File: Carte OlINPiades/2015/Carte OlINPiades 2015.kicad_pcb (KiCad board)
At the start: 2 copper layers, 284 parts, among them U1 dsPIC33FJ128MC802, U2 LM7805, U3 LM2937-3.3

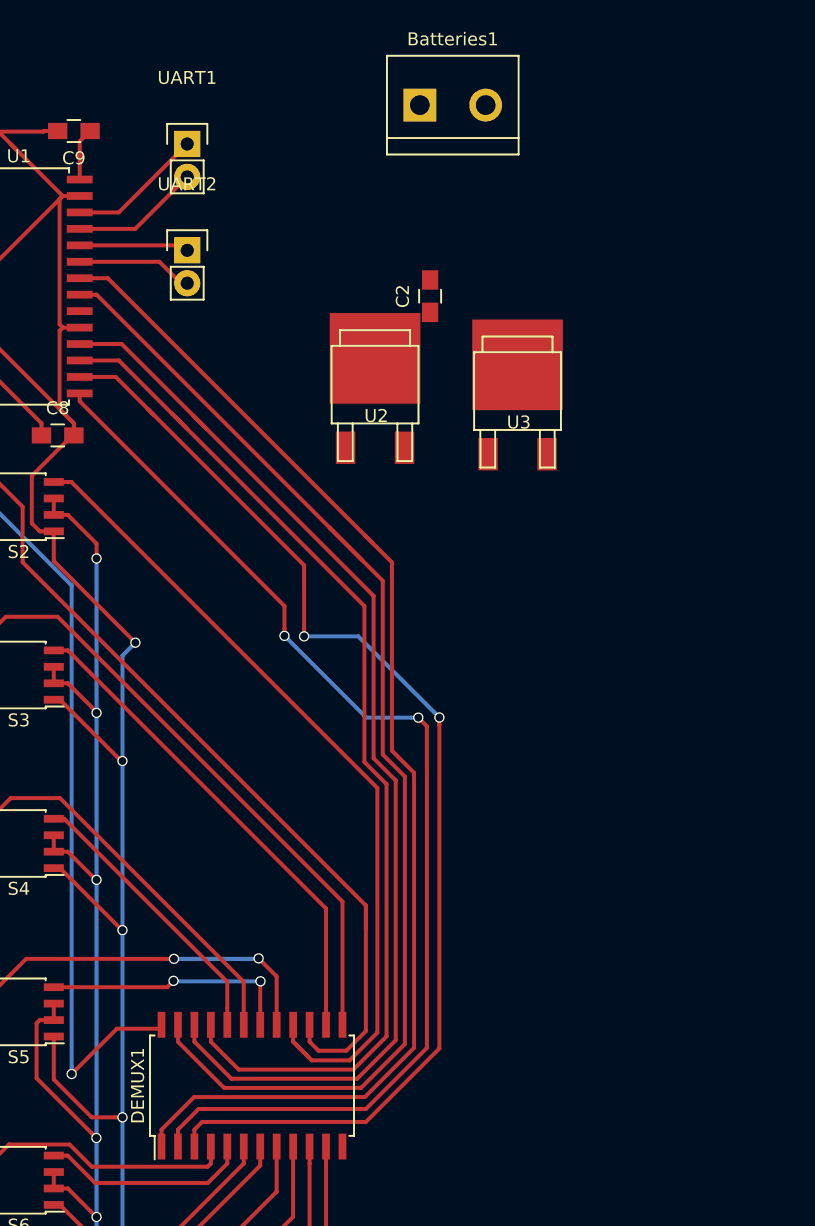
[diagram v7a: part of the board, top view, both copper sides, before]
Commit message: ajoute pistes capa tantale
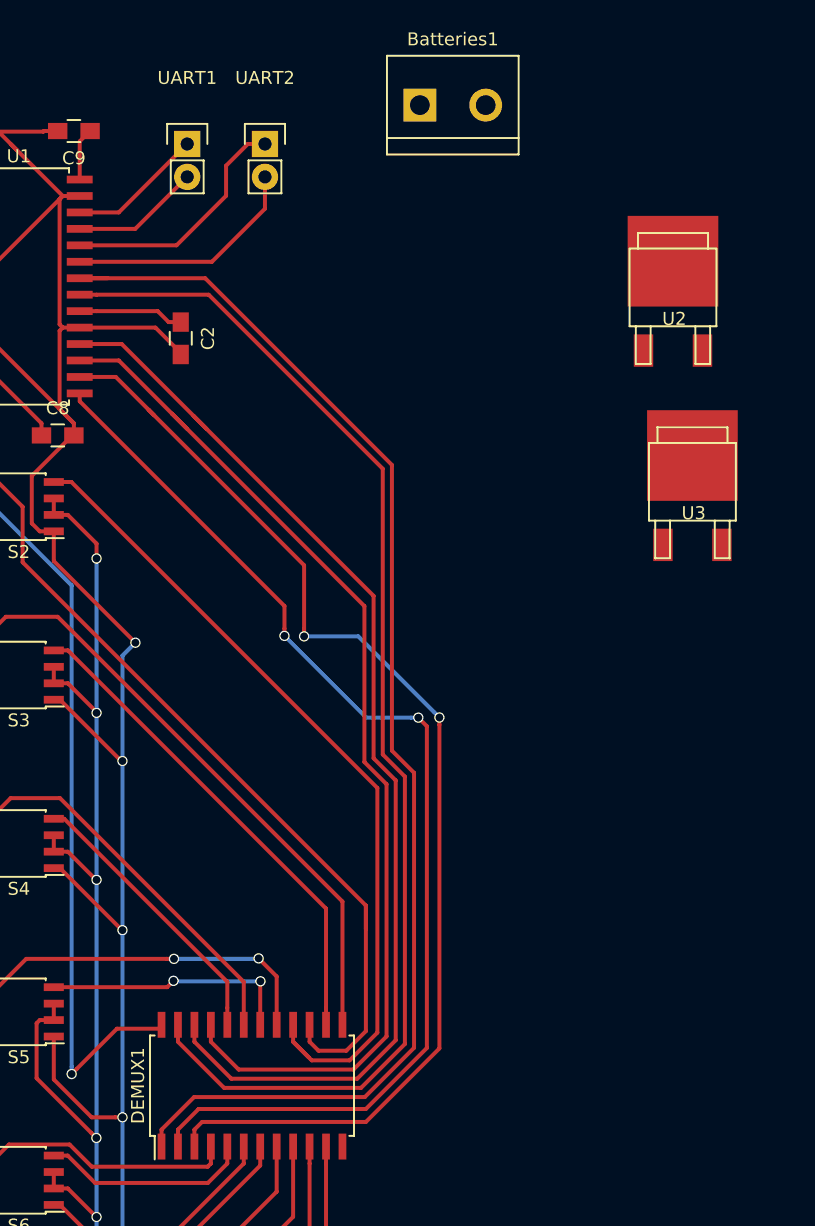
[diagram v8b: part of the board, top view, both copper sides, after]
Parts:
- moved U2 24.2 mm to (207.5, 52.0)
- moved C2 19.5 mm to (169.5, 54.5), turned to 270 degrees
- moved U3 15.2 mm to (209.0, 67.0)
- moved UART2 10.2 mm to (176.0, 39.5)
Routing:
- net RB13: track 8.46 -> 18.9 mm
- net RB12: track 8.99 -> 18.5 mm
- net GND: track 350.3 -> 359.1 mm
- net Net-(C2-Pad1): track 0.00 -> 8.15 mm
- net RB11: track 95.5 -> 101.4 mm
- net RB10: track 94.3 -> 95.8 mm
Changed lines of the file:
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@@
     (thickness 1.6)
     (drawings 0)
-    (tracks 1461)
+    (tracks 1469)
     (zones 0)
     (modules 284)
@@
   )
   (module Capacitors_SMD:C_0805_HandSoldering (layer F.Cu)
-    (at 188.75 51.25 90)
+    (at 169.5 54.5 270)
     (descr "Capacitor SMD 0805, hand soldering")
     (tags "capacitor 0805")
     (attr smd)
-    (fp_text reference C2 (at 0 -2.1 90) (layer F.SilkS)
+    (fp_text reference C2 (at 0 -2.1 270) (layer F.SilkS)
       (effects (font (size 1 1) (thickness 0.15)))
     )
-    (fp_text value 10uF (at 0 2.1 90) (layer F.Fab)
+    (fp_text value 10uF (at 0 2.1 270) (layer F.Fab)
       (effects (font (size 1 1) (thickness 0.15)))
     )
@@
     (fp_line (start 0.5 -0.85) (end -0.5 -0.85) (layer F.SilkS) (width 0.15))
     (fp_line (start -0.5 0.85) (end 0.5 0.85) (layer F.SilkS) (width 0.15))
-    (pad 1 smd rect (at -1.25 0 90) (size 1.5 1.25) (layers F.Cu F.Paste F.Mask)
+    (pad 1 smd rect (at -1.25 0 270) (size 1.5 1.25) (layers F.Cu F.Paste F.Mask)
       (net 4 "Net-(C2-Pad1)"))
-    (pad 2 smd rect (at 1.25 0 90) (size 1.5 1.25) (layers F.Cu F.Paste F.Mask)
+    (pad 2 smd rect (at 1.25 0 270) (size 1.5 1.25) (layers F.Cu F.Paste F.Mask)
       (net 2 GND))
     (model Capacitors_SMD.3dshapes/C_0805_HandSoldering.wrl
@@
   )
   (module Transistors_SMD:sot428 (layer F.Cu)
-    (at 184.5 59.5)
+    (at 207.5 52)
     (descr SOT428)
     (attr smd)
@@
   )
   (module Transistors_SMD:sot428 (layer F.Cu)
-    (at 195.5 60)
+    (at 209 67)
     (descr SOT428)
     (attr smd)
@@
   )
   (module Pin_Headers:Pin_Header_Straight_1x02 (layer F.Cu)
-    (at 170 47.71)
+    (at 176 39.5)
     (descr "Through hole pin header")
     (tags "pin header")
@@
     )
   )
+  (segment (start 161.7 53.675) (end 167.55 53.675) (width 0.308) (layer F.Cu) (net 2))
+  (segment (start 167.55 53.675) (end 169.5 55.625) (width 0.308) (layer F.Cu) (net 2))
+  (segment (start 169.5 55.625) (end 169.5 55.75) (width 0.308) (layer F.Cu) (net 2))
   (segment (start 158 65.125) (end 158 68.788) (width 0.308) (layer F.Cu) (net 2))
   (segment (start 158 68.788) (end 158.617 69.405) (width 0.308) (layer F.Cu) (net 2))
@@
   (segment (start 125.317 39.5) (end 130.2484 39.5) (width 0.308) (layer F.Cu) (net 3))
   (segment (start 130.2484 39.5) (end 131.42 39.5) (width 0.308) (layer F.Cu) (net 3))
+  (segment (start 169.5 53.25) (end 168.567 53.25) (width 0.308) (layer F.Cu) (net 4))
+  (segment (start 168.567 53.25) (end 167.722 52.405) (width 0.308) (layer F.Cu) (net 4))
+  (segment (start 167.722 52.405) (end 163.008 52.405) (width 0.308) (layer F.Cu) (net 4))
+  (segment (start 163.008 52.405) (end 161.7 52.405) (width 0.308) (layer F.Cu) (net 4))
   (segment (start 149.135 66.865) (end 146.27 64) (width 0.308) (layer F.Cu) (net 6))
   (segment (start 154.3 66.865) (end 149.135 66.865) (width 0.308) (layer F.Cu) (net 6))
@@
   (segment (start 164.715 56.215) (end 168.828091 60.328091) (width 0.308) (layer F.Cu) (net 47))
   (segment (start 168.828091 60.328091) (end 170 61.5) (width 0.308) (layer F.Cu) (net 47))
-  (segment (start 185.095032 73.222032) (end 180.979371 69.106371) (width 0.308) (layer F.Cu) (net 48))
+  (segment (start 163.008 51.135) (end 161.7 51.135) (width 0.308) (layer F.Cu) (net 48))
+  (segment (start 185.095032 64.572658) (end 171.657374 51.135) (width 0.308) (layer F.Cu) (net 48))
+  (segment (start 185.095032 86.630932) (end 185.095032 64.572658) (width 0.308) (layer F.Cu) (net 48))
+  (segment (start 186.80304 88.33894) (end 185.095032 86.630932) (width 0.308) (layer F.Cu) (net 48))
+  (segment (start 186.80304 108.984274) (end 186.80304 88.33894) (width 0.308) (layer F.Cu) (net 48))
   (segment (start 183.417291 112.370023) (end 186.80304 108.984274) (width 0.308) (layer F.Cu) (net 48))
-  (segment (start 169.285 108.808) (end 172.847023 112.370023) (width 0.308) (layer F.Cu) (net 48))
   (segment (start 172.847023 112.370023) (end 183.417291 112.370023) (width 0.308) (layer F.Cu) (net 48))
+  (segment (start 169.285 108.808) (end 172.847023 112.370023) (width 0.308) (layer F.Cu) (net 48))
+  (segment (start 171.657374 51.135) (end 163.008 51.135) (width 0.308) (layer F.Cu) (net 48))
   (segment (start 169.285 107.5) (end 169.285 108.808) (width 0.308) (layer F.Cu) (net 48))
-  (segment (start 186.80304 108.984274) (end 186.80304 88.33894) (width 0.308) (layer F.Cu) (net 48))
-  (segment (start 185.095032 86.630932) (end 185.095032 73.222032) (width 0.308) (layer F.Cu) (net 48))
-  (segment (start 186.80304 88.33894) (end 185.095032 86.630932) (width 0.308) (layer F.Cu) (net 48))
-  (segment (start 163.008 51.135) (end 180.979371 69.106371) (width 0.308) (layer F.Cu) (net 48))
-  (segment (start 180.979371 69.106371) (end 183.5 71.627) (width 0.308) (layer F.Cu) (net 48))
-  (segment (start 161.7 51.135) (end 163.008 51.135) (width 0.308) (layer F.Cu) (net 48))
   (segment (start 184.67901 108.10447) (end 184.67901 89.218744) (width 0.308) (layer F.Cu) (net 49))
   (segment (start 161.055266 65.595) (end 160.783 65.595) (width 0.308) (layer F.Cu) (net 49))
@@
   (segment (start 138.57748 53.675) (end 132.22748 47.325) (width 0.308) (layer F.Cu) (net 61))
   (segment (start 152.3 53.675) (end 138.57748 53.675) (width 0.308) (layer F.Cu) (net 61))
-  (segment (start 185.803042 71.803042) (end 183.781141 69.781141) (width 0.308) (layer F.Cu) (net 75))
-  (segment (start 187.51105 88.045672) (end 185.803043 86.337665) (width 0.308) (layer F.Cu) (net 75))
-  (segment (start 185.803043 86.337665) (end 185.803042 71.803042) (width 0.308) (layer F.Cu) (net 75))
-  (segment (start 183.710559 113.078033) (end 187.51105 109.277542) (width 0.308) (layer F.Cu) (net 75))
-  (segment (start 187.51105 109.277542) (end 187.51105 88.045672) (width 0.308) (layer F.Cu) (net 75))
-  (segment (start 168.015 115.592) (end 170.528967 113.078033) (width 0.308) (layer F.Cu) (net 75))
-  (segment (start 168.015 116.9) (end 168.015 115.592) (width 0.308) (layer F.Cu) (net 75))
-  (segment (start 170.528967 113.078033) (end 183.710559 113.078033) (width 0.308) (layer F.Cu) (net 75))
-  (segment (start 184.255022 70.255022) (end 183.781141 69.781141) (width 0.308) (layer F.Cu) (net 75))
-  (segment (start 183.781141 69.781141) (end 163.865 49.865) (width 0.308) (layer F.Cu) (net 75))
+  (segment (start 185.803043 64.279391) (end 185.803043 86.337665) (width 0.308) (layer F.Cu) (net 75))
+  (segment (start 170.528967 113.078033) (end 168.015 115.592) (width 0.308) (layer F.Cu) (net 75))
+  (segment (start 161.7 49.865) (end 171.388652 49.865) (width 0.308) (layer F.Cu) (net 75))
+  (segment (start 171.388652 49.865) (end 185.803043 64.279391) (width 0.308) (layer F.Cu) (net 75))
+  (segment (start 187.51105 109.277542) (end 183.710559 113.078033) (width 0.308) (layer F.Cu) (net 75))
+  (segment (start 185.803043 86.337665) (end 187.51105 88.045672) (width 0.308) (layer F.Cu) (net 75))
+  (segment (start 183.710559 113.078033) (end 170.528967 113.078033) (width 0.308) (layer F.Cu) (net 75))
+  (segment (start 187.51105 88.045672) (end 187.51105 109.277542) (width 0.308) (layer F.Cu) (net 75))
+  (segment (start 168.015 115.592) (end 168.015 116.9) (width 0.308) (layer F.Cu) (net 75))
   (segment (start 163.865 49.865) (end 161.7 49.865) (width 0.308) (layer F.Cu) (net 75))
-  (segment (start 161.7 48.595) (end 167.855798 48.595) (width 0.308) (layer F.Cu) (net 76))
-  (segment (start 167.855798 48.595) (end 169.510798 50.25) (width 0.308) (layer F.Cu) (net 76))
-  (segment (start 169.510798 50.25) (end 170 50.25) (width 0.308) (layer F.Cu) (net 76))
-  (segment (start 161.7 47.325) (end 169.615 47.325) (width 0.308) (layer F.Cu) (net 77))
-  (segment (start 169.615 47.325) (end 170 47.71) (width 0.308) (layer F.Cu) (net 77))
+  (segment (start 161.7 48.595) (end 171.905 48.595) (width 0.308) (layer F.Cu) (net 76))
+  (segment (start 171.905 48.595) (end 176 44.5) (width 0.308) (layer F.Cu) (net 76))
+  (segment (start 176 44.5) (end 176 42.04) (width 0.308) (layer F.Cu) (net 76))
+  (segment (start 173 43.5) (end 169.175 47.325) (width 0.308) (layer F.Cu) (net 77))
+  (segment (start 169.175 47.325) (end 161.7 47.325) (width 0.308) (layer F.Cu) (net 77))
+  (segment (start 173 41.176) (end 173 43.5) (width 0.308) (layer F.Cu) (net 77))
+  (segment (start 176 39.5) (end 174.676 39.5) (width 0.308) (layer F.Cu) (net 77))
+  (segment (start 174.676 39.5) (end 173 41.176) (width 0.308) (layer F.Cu) (net 77))
   (segment (start 161.7 46.055) (end 165.985 46.055) (width 0.308) (layer F.Cu) (net 78))
   (segment (start 165.985 46.055) (end 170 42.04) (width 0.308) (layer F.Cu) (net 78))
